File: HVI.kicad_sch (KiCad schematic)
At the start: 36 parts, among them J1 Conn_01x02, J2 Conn_01x02, J3 Conn_01x02, U1 VIPER06-SSOP-10

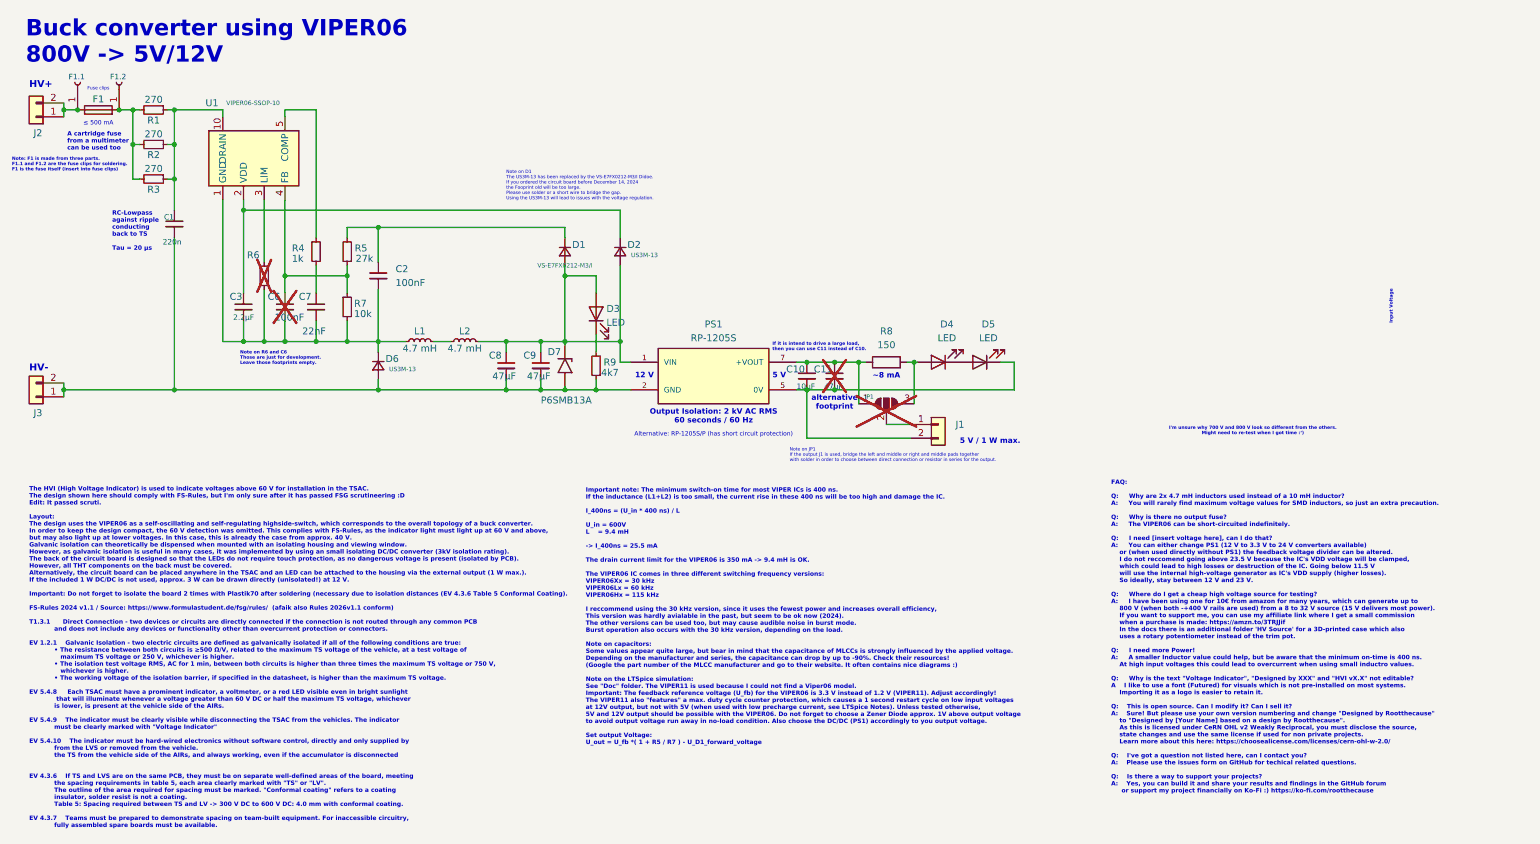
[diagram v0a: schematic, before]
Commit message: Changed the connectors to Molex MicrofitPlus
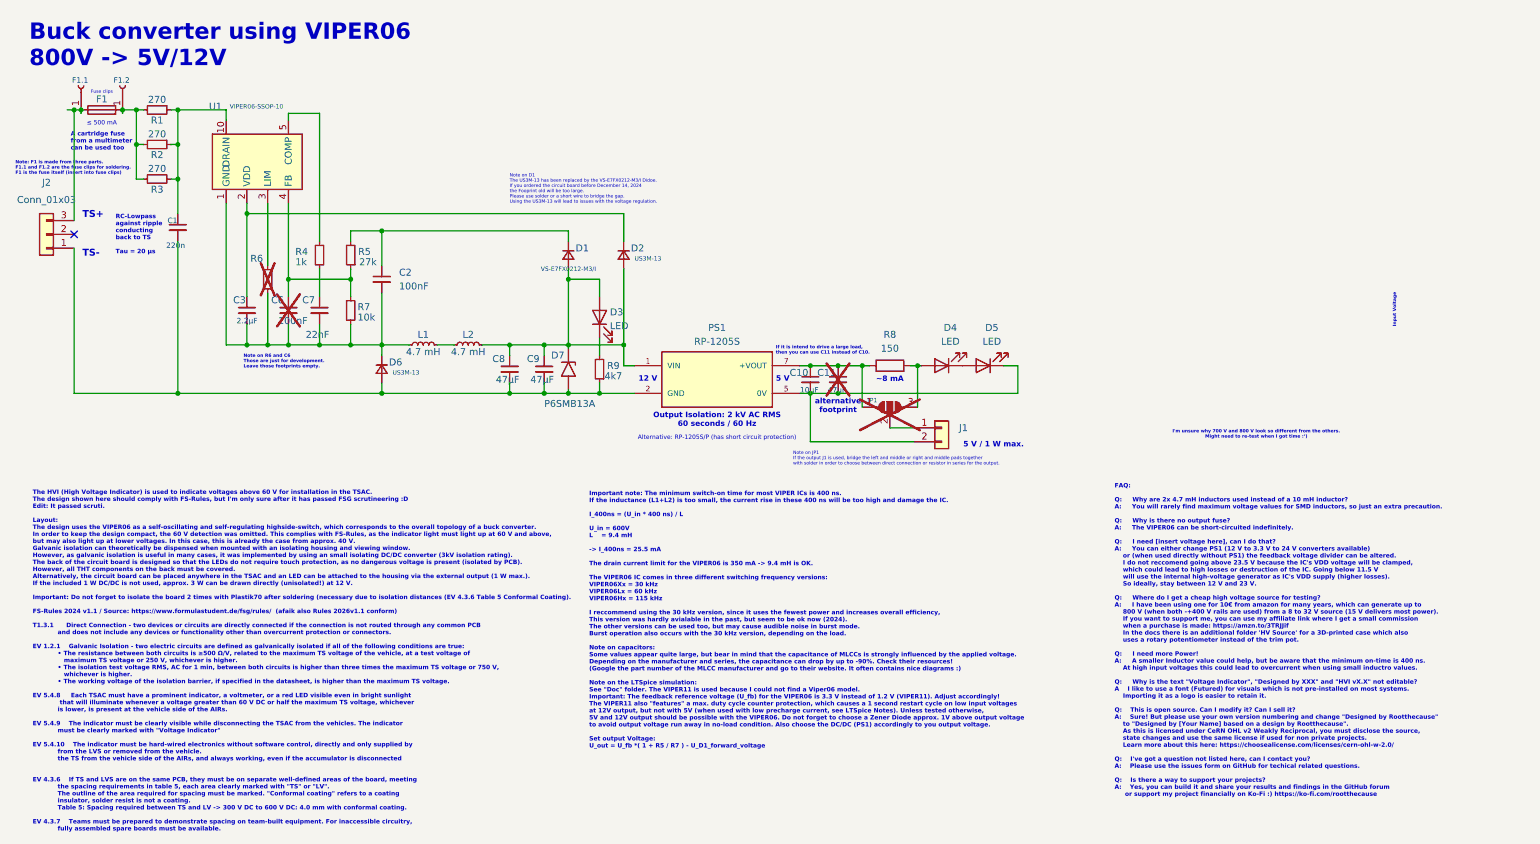
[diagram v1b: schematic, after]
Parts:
- removed J2, J3: Conn_01x02, Connector_Molex:Molex_Micro-Fit_3.0_43650-0215_1x02_P3.00mm_Vertical, symbol Connector_Generic:Conn_01x02
- added J2: Conn_01x03, yfs:MolexMicrofitPlus1x3, symbol Connector_Generic:Conn_01x03
- J1: footprint Connector_Molex:Molex_Micro-Fit_3.0_43650-0215_1x02_P3.00mm_Vertical -> yfs:MolexMicrofitPlus1x2
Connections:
- net at C1.2, C8.2, C9.2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: now also J2.1 (Pin_1)
- net at F1.1, F1.1.1 (Pin_1): now also J2.3 (Pin_3)
- no-connect marks 0 -> 1
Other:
- note added: "TS+"
- note added: "TS-"
- note removed: "HV+"
- note removed: "HV-"
- moved on the sheet: C1, C10, C11, C2, C3, C6, C7, C8, C9, D1, D2, D3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

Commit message: Changed the DC/DC converter to 12V/12V, and updated the labels for the pin
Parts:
- PS1: value RP-1205S -> DRS1-12-S12-S
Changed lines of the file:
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@@
 			)
 		)
-		(property "Value" "RP-1205S"
+		(property "Value" "DRS1-12-S12-S"
 			(at 142.24 75.565 0)
 			(effects
@@
 			)
 		)
-		(property "Datasheet" "https://www.mouser.de/ProductDetail/RECOM-Power/RP-1205S?qs=8OBu2JtKQqq6GIat8AjVyQ%3D%3D"
+		(property "Datasheet" "https://www.mouser.co.uk/ProductDetail/CUI-Inc/DRS1-12-S12-S?qs=sGAEpiMZZMsc0tfZmXiUnTr9pnMRotOJRoPmEQ7ig4f1IrxG7ygsQw%3D%3D"
 			(at 142.24 82.55 0)
 			(effects
@@
 		)
 		(instances
-			(project ""
+			(project "HVI"
 				(path "/96589b0c-b051-494a-952b-1d85eb492735"
 					(reference "J2")
@@
 		)
 		(instances
-			(project ""
+			(project "HVI"
 				(path "/96589b0c-b051-494a-952b-1d85eb492735"
 					(reference "F1.1")

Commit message: Added the footprint of the new DC/DC converter and moved around the PCB a tad
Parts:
- PS1: footprint Converter_DCDC:CONV_PEME1-S5-S5-S -> yfs:DCDC-12v_12v-DRS1-12-S12-S
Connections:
- net at C10.2, C11.2, D5.1 (K)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: now also PS1.3 (-VOUT); no longer PS1.5 (-VOUT)
- net at C10.1, C11.1, JP1.1 (A)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: now also PS1.4 (+VOUT); no longer PS1.7 (+VOUT)
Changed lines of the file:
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@@
 			)
 		)
-		(property "Footprint" "Converter_DCDC:CONV_PEME1-S5-S5-S"
+		(property "Footprint" "yfs:DCDC-12v_12v-DRS1-12-S12-S"
 			(at 142.24 82.55 0)
 			(effects
@@
 		(pin "2"
 		)
-		(pin "5"
+		(pin "3"
 		)
-		(pin "7"
+		(pin "4"
 		)
 		(instances

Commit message: Changed the fuse
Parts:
- F1: footprint DC-DC Footprint Lib:Fuseholder0,25Zoll_32mm_littlefuse_102_122 -> Fuse:Fuseholder_Clip-5x20mm_Keystone_3512_Inline_P23.62x7.27mm_D1.02x1.57mm_Horizontal
